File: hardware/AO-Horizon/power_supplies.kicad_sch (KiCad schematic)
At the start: 28 parts

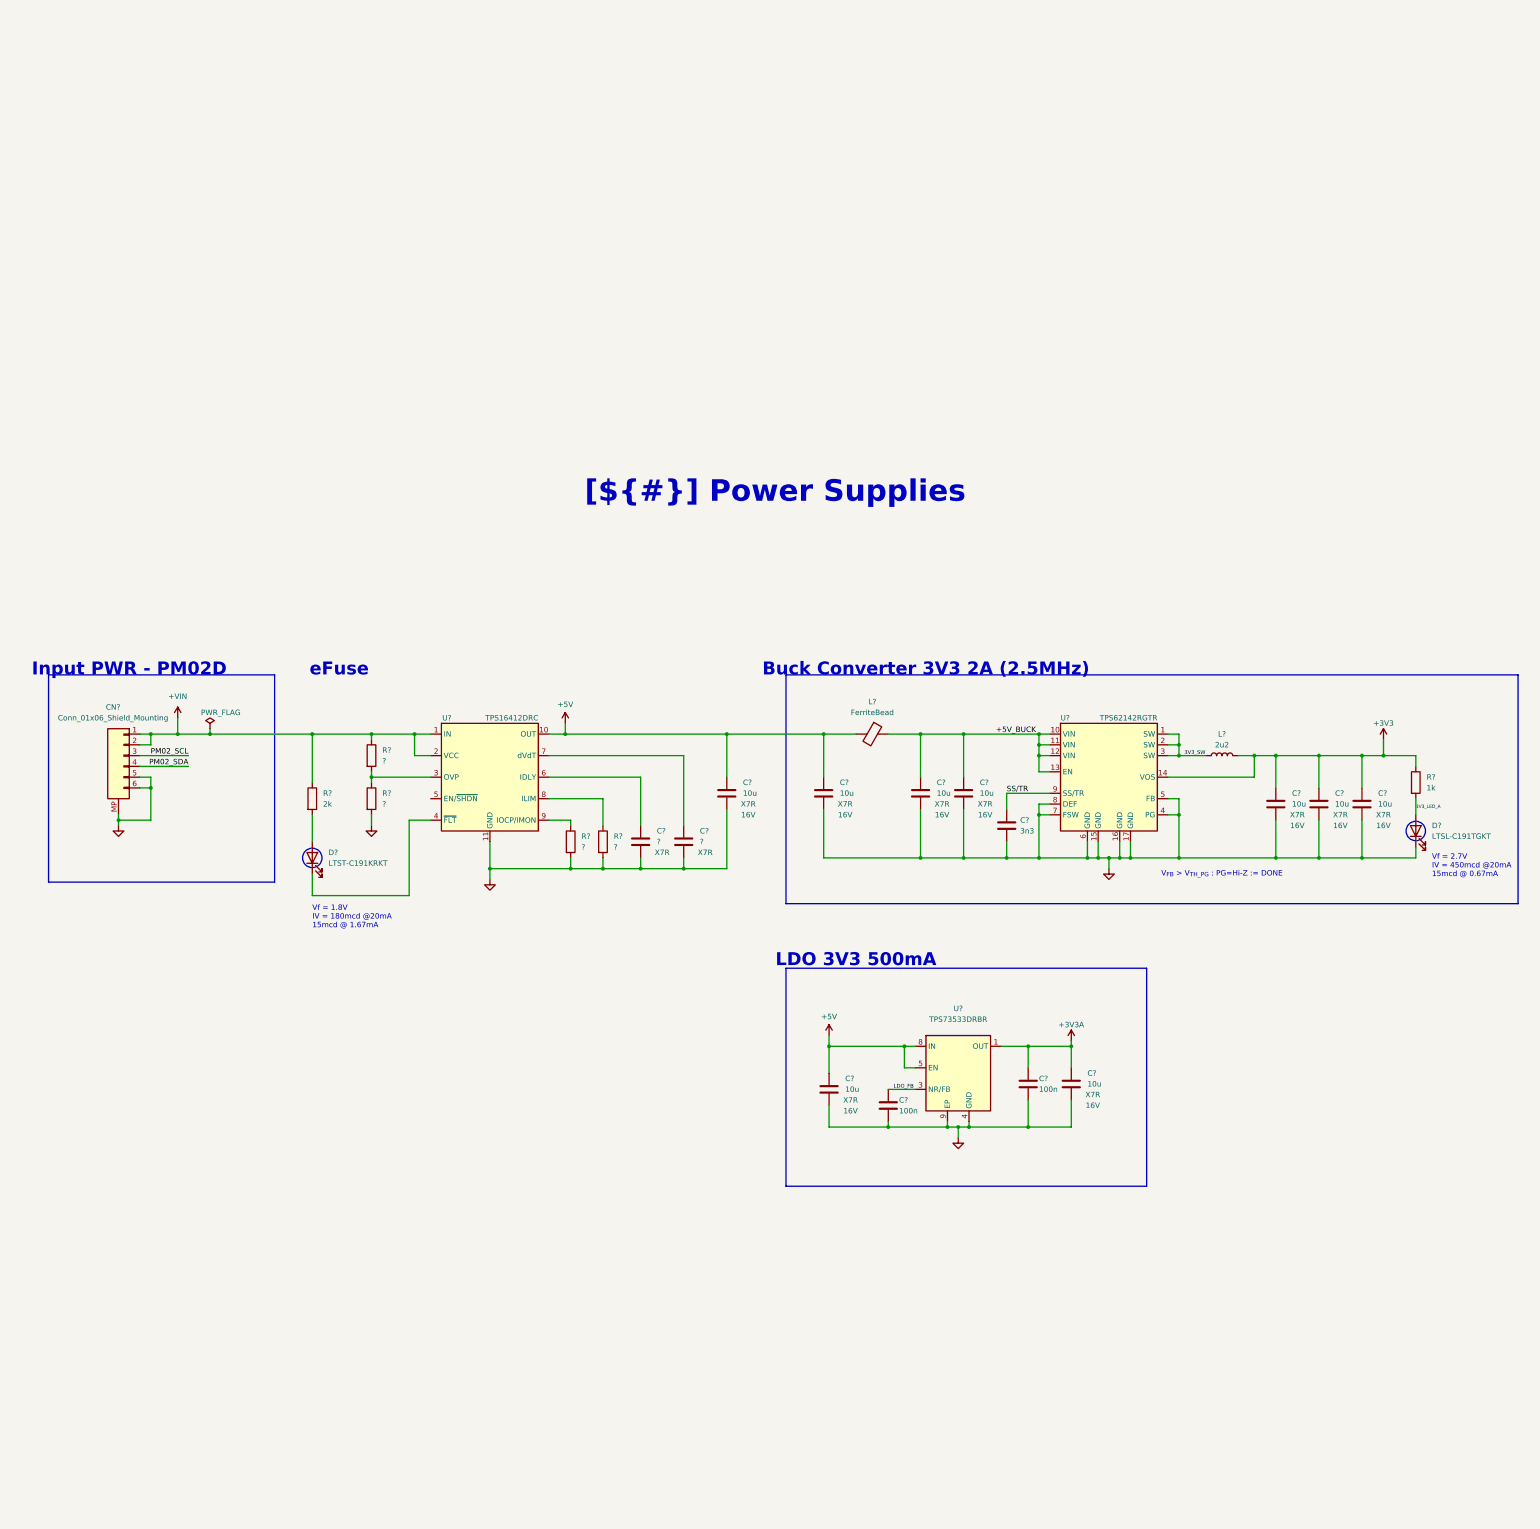
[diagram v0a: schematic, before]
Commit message: feat(schematic): add TPS25924 eFuse stage to the power sheet
Adds one TPS25924xDRC with 10 capacitors, 4 resistors and a Zener diode,
FUSE_* net labels, and the PM02_SCL and PM02_SDA global labels.

ERC: NOT_VERIFIED.

Co-Authored-By: Claude Opus 5.5 <noreply@anthropic.com>
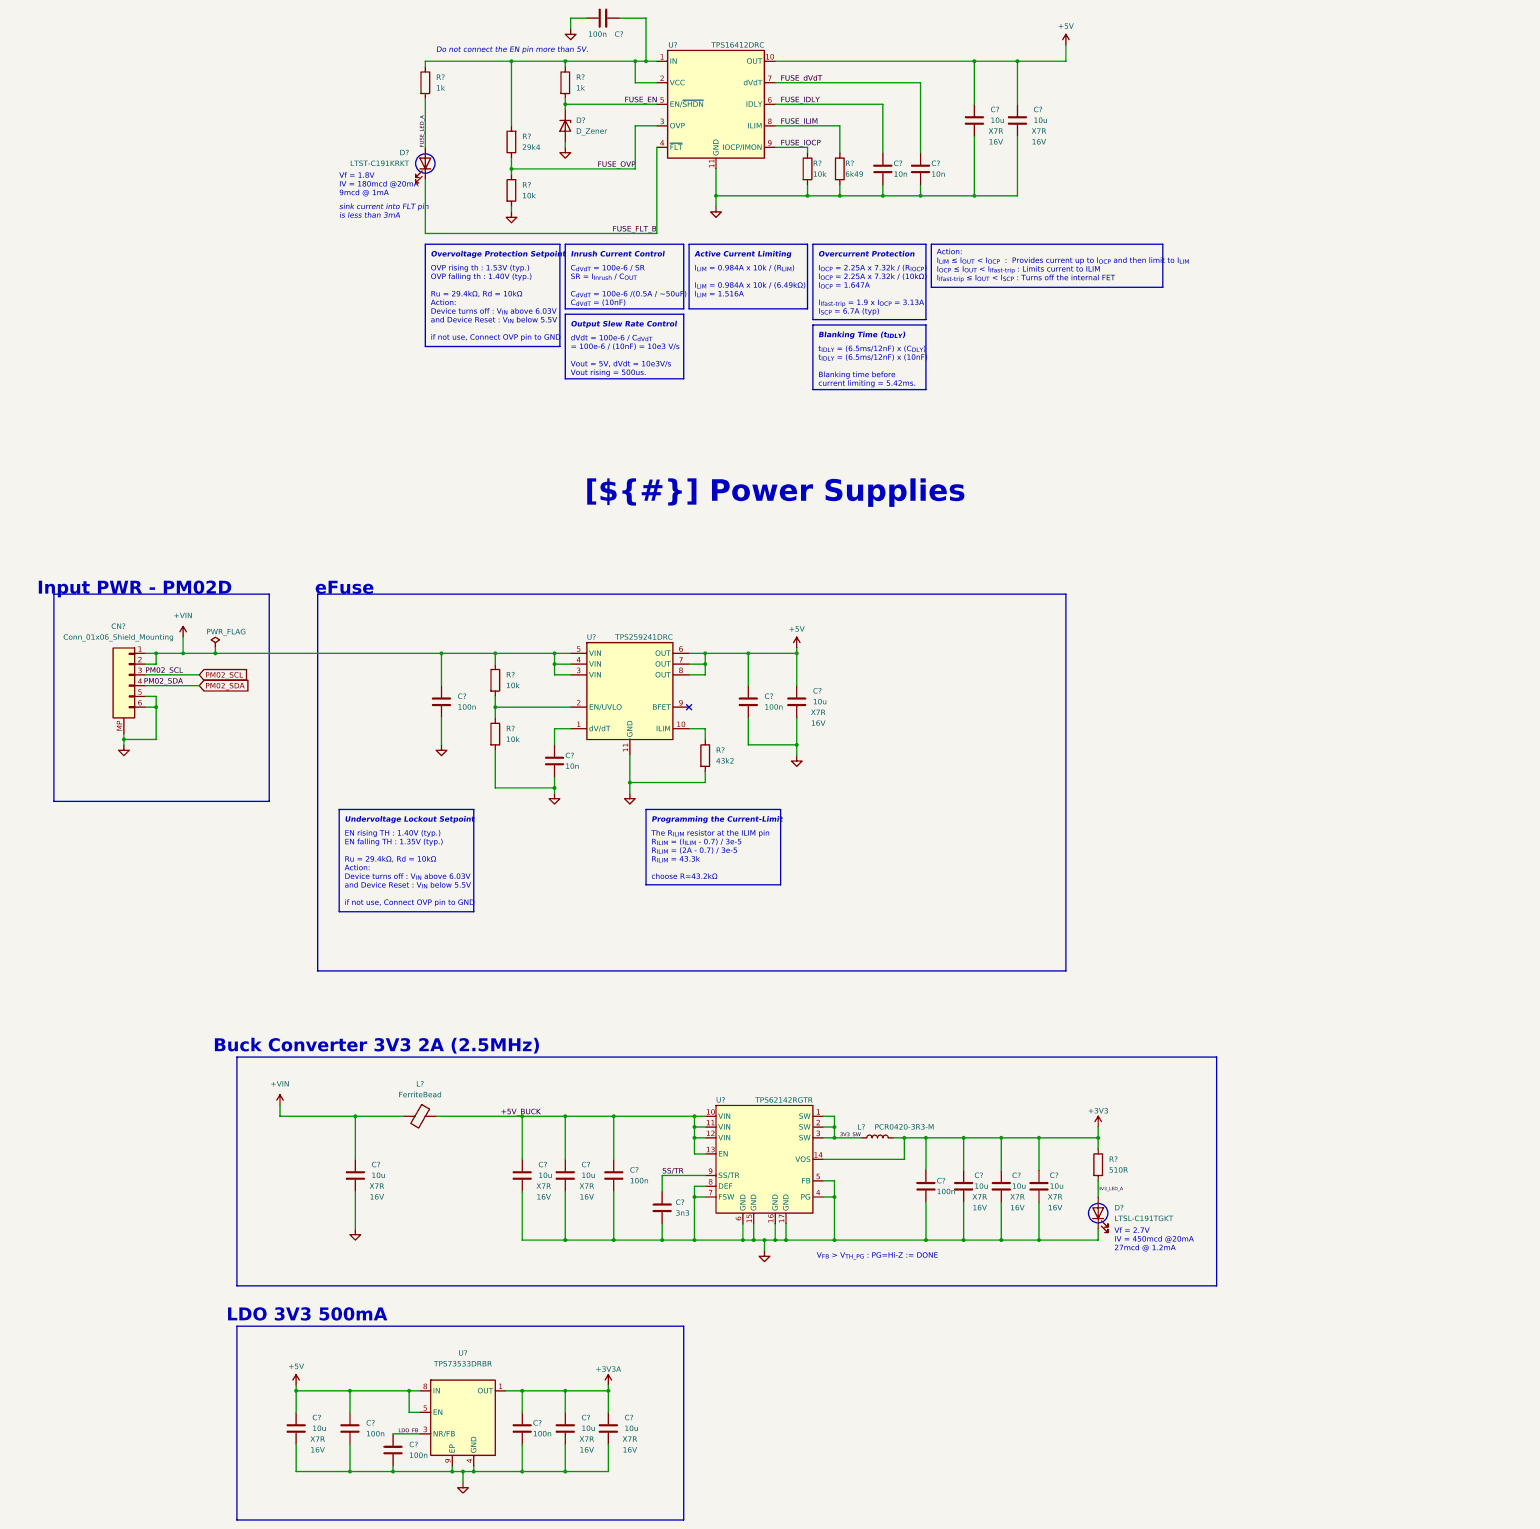
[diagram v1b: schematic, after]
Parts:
- removed C? (x2): 100n, 0_Capacitor_SMD:C_0603_1608Metric_NomDensity, symbol Device:C
- removed C? (x8): 10u, 0_Capacitor_SMD:C_0805_2012Metric_NomDensity, symbol Device:C
- removed C? (x2): ?, symbol Device:C
- removed R?: 1k, 0_Resistor_SMD:R_0603_1608Metric_NomDensity, symbol Device:R
- removed R? (x4): ?, 0_Resistor_SMD:R_0603_1608Metric_NomDensity, symbol Device:R
- removed R?: 2k, 0_Resistor_SMD:R_0603_1608Metric_NomDensity, symbol Device:R
- added C? (x11): 10u, 0_Capacitor_SMD:C_0805_2012Metric_NomDensity, symbol Device:C
- added C? (x8): 100n, 0_Capacitor_SMD:C_0402_1005Metric_NomDensity, symbol Device:C
- added C? (x3): 10n, symbol Device:C
- added D?: D_Zener, symbol Device:D_Zener
- added R? (x2): 1k, symbol Device:R
- added R? (x4): 10k, symbol Device:R
- added R?: 510R, symbol Device:R
- added R?: 6k49, symbol Device:R
- added R?: 29k4, symbol Device:R
- added R?: 43k2, symbol Device:R
- added U?: TPS259241DRC, 0_Package_SON:Texas_VSON-10-1EP_3x3mm_P0.5mm_EP1.65x2.4mm_ThermalVias, symbol 0_Protection_eFuse:TPS25924xDRC
- C?: MFR.P/N (none) -> GRM1885C1H332JA01D; MPN GRM1885C1H332JA01D -> (none)
- C?: MFR.P/N (none) -> GRM21BZ71C106KE15L; MPN GRM21BZ71C106KE15L -> (none)
- L?: value 2u2 -> PCR0420-3R3-M; footprint 0_Inductor_SMD:L_Abracon_AOTA-B252010S -> 0_Inductor_SMD:L_JIERR_PCR0420; LCSC C19271752 -> C53896857; MFR ABRACON -> JIERR; MFR.P/N (none) -> PCR0420-3R3-M; MPN AOTA-B252010S2R2MT -> (none)
- U?: MFR.P/N (none) -> TPS73533DRBR; MPN TPS73533DRBR -> (none)
- U?: MFR.P/N (none) -> TPS62142RGTR; MPN TPS62142RGTR -> (none)
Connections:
- net +3V3: now also C?.1, C?.1, C?.1, C?.1, R?.1
- net +3V3A: now also C?.1, C?.1, C?.1
- net +5V: now also C?.1, C?.1, C?.1, C?.1, C?.1, C?.1, U?.6 (OUT), U?.7 (OUT), U?.8 (OUT); no longer L?.2
- net +5V_BUCK: now also C?.1, C?.1
- net +VIN: now also L?.2, C?.1, C?.1, R?.1, U?.3 (VIN), U?.4 (VIN), U?.5 (VIN); no longer U?.1 (IN), U?.2 (VCC)
- net 3V3_LED_A: now also R?.2
- net GND: now also C?.2, C?.2, C?.2, C?.2, C?.2, C?.2, C?.2, C?.2, C?.2, C?.2, C?.2, C?.2, C?.2, C?.2, C?.2, C?.2, C?.2, C?.2, C?.2, C?.2, C?.2, C?.2, D?.2 (A), R?.2, R?.2, R?.2, R?.2, R?.2, U?.11 (GND)
- net LDO_FB: now also C?.1
- net FUSE_OVP: now reaches U?.3 (OVP)
- net FUSE_OVP: now also R?.1, R?.1
- net FUSE_FLT_B: now reaches D?.1 (K), U?.4 (~{FLT})
- net FUSE_EN: now reaches U?.5 (EN/~{SHDN})
- net FUSE_EN: now also D?.1 (K), R?.2
- net FUSE_IDLY: now reaches U?.6 (IDLY)
- net FUSE_IDLY: now also C?.1
- net FUSE_dVdT: now reaches U?.7 (dVdT)
- net FUSE_dVdT: now also C?.1
- net FUSE_ILIM: now reaches U?.8 (ILIM)
- net FUSE_ILIM: now also R?.1
- net FUSE_IOCP: now reaches U?.9 (IOCP/IMON)
- net FUSE_IOCP: now also R?.1
- net FUSE_LED_A: now reaches D?.2 (A)
- net FUSE_LED_A: now also R?.2
- new net: C?.1, R?.1, R?.1, R?.2, U?.1 (IN), U?.2 (VCC)
- new net: C?.1, U?.1 (dV/dT)
- new net: R?.1, U?.10 (ILIM)
- new net: R?.1, R?.2, U?.2 (EN/UVLO)
- no-connect marks 0 -> 1
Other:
- note added: "Action: I_{LIM} ≤ I_{OUT} < I_{OCP} : Provides current up to I_{OCP} and then limit to I_{LIM} I_{OCP} ≤ I_{OUT} < I_{Ifast-trip} : Limits current to ILIM I_{Ifast-trip} ≤ I_{OUT} < I_{SCP} : Turns off the internal FET"
- note added: "Active Current Limiting"
- note added: "Blanking Time (t_{IDLY})"
- note added: "C_{dVdT} = 100e-6 / SR SR = I_{Inrush} / C_{OUT} C_{dVdT} = 100e-6 /(0.5A / ~50uF) C_{dVdT} = (10nF)"
- note added: "Do not connect the EN pin more than 5V."
- note added: "EN rising TH : 1.40V (typ.) EN falling TH : 1.35V (typ.) Ru = 29.4kΩ, Rd = 10kΩ Action: Device turns off : V_{IN} above 6.03V and Device Reset : V_{IN} below 5.5V if not use, Connect OVP pin to GND"
- note added: "I_{LIM} = 0.984A x 10k / (R_{LIM}) I_{LIM} = 0.984A x 10k / (6.49kΩ) I_{LIM} = 1.516A"
- note added: "I_{OCP} = 2.25A x 7.32k / (R_{IOCP}) I_{OCP} = 2.25A x 7.32k / (10kΩ) I_{OCP} = 1.647A I_{Ifast-trip} = 1.9 x I_{OCP} = 3.13A I_{SCP} = 6.7A (typ)"
- note added: "Inrush Current Control"
- note added: "OVP rising th : 1.53V (typ.) OVP falling th : 1.40V (typ.) Ru = 29.4kΩ, Rd = 10kΩ Action: Device turns off : V_{IN} above 6.03V and Device Reset : V_{IN} below 5.5V if not use, Connect OVP pin to GND"
- note added: "Output Slew Rate Control"
- note added: "Overcurrent Protection"
- note added: "Overvoltage Protection Setpoint"
- note added: "Programming the Current-Limit"
- note added: "The R_{ILIM} resistor at the ILIM pin R_{ILIM} = (I_{ILIM} - 0.7) / 3e-5 R_{ILIM} = (2A - 0.7) / 3e-5 R_{ILIM} = 43.3k choose R=43.2kΩ"
- note added: "Undervoltage Lockout Setpoint"
- note added: "Vf = 1.8V IV = 180mcd @20mA 9mcd @ 1mA"
- note added: "Vf = 2.7V IV = 450mcd @20mA 27mcd @ 1.2mA"
- note added: "dVdt = 100e-6 / C_{dVdT} = 100e-6 / (10nF) = 10e3 V/s Vout = 5V, dVdt = 10e3V/s Vout rising = 500us."
- note added: "sink current into FLT pin is less than 3mA"
- note added: "t_{IDLY} = (6.5ms/12nF) x (C_{DLY}) t_{IDLY} = (6.5ms/12nF) x (10nF) Blanking time before current limiting = 5.42ms."
- note removed: "Vf = 1.8V IV = 180mcd @20mA 15mcd @ 1.67mA"
- note removed: "Vf = 2.7V IV = 450mcd @20mA 15mcd @ 0.67mA"
- moved on the sheet: C?, CN?, D?, L?, U?
